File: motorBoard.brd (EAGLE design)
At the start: 160 x 100 mm, 58 parts

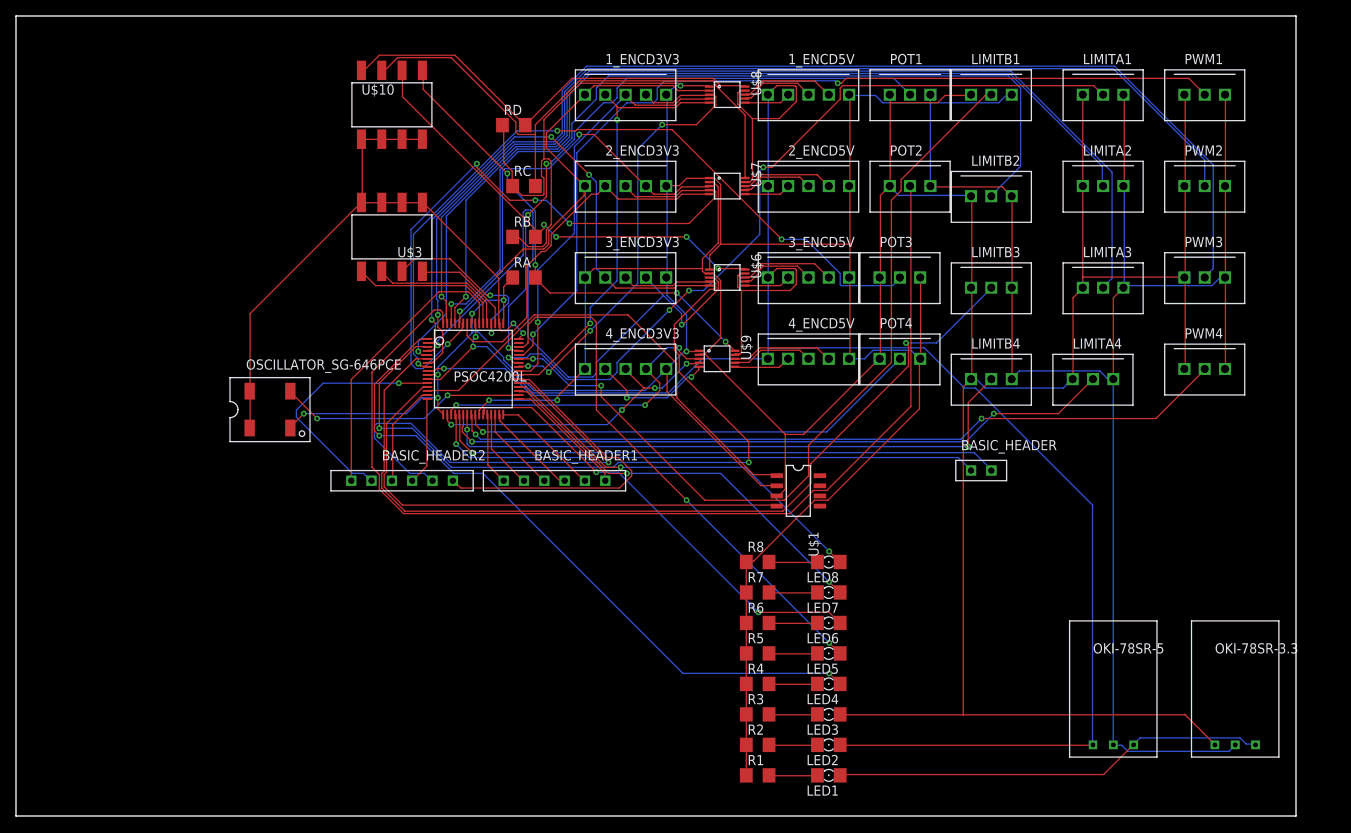
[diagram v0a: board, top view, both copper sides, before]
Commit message: Added decoupling caps, schematic tweaks, layout, mid routing
Running out of space around PSoC, so I need to rework my component layout.
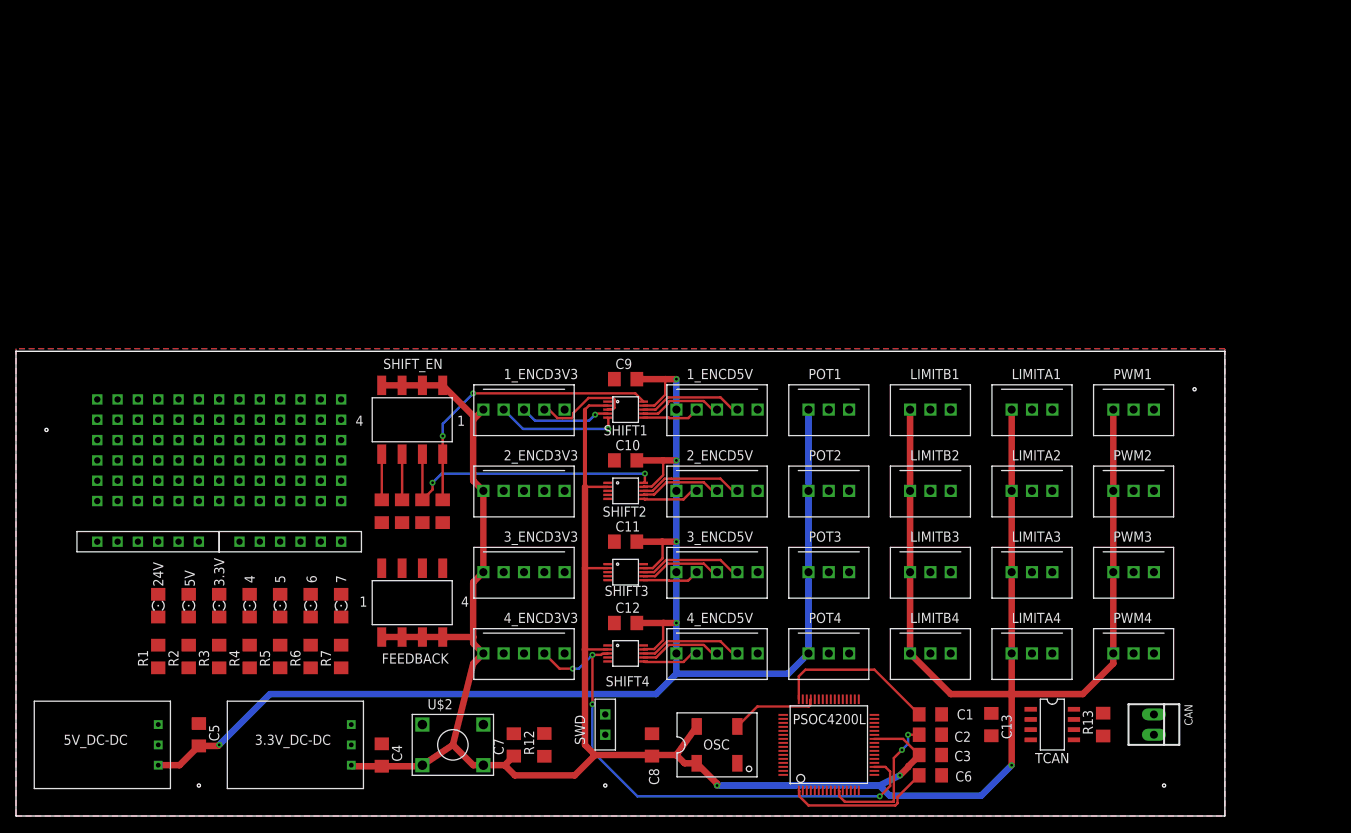
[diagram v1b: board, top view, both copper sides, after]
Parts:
- removed BASIC_HEADER: 2BASIC_HEADER, HuskyRobotics2017-18:2SIP_HEADER
- removed LED1, LED2, LED3, LED4, LED5, LED6, LED7, LED8: (no value), eagle-ltspice:LED_1206
- removed OKI-78SR-3.3: OKI-78SR-3.33SIP, HuskyRobotics2017-18:3SIP
- removed OKI-78SR-5: OKI-78SR-53SIP, HuskyRobotics2017-18:3SIP
- removed OSCILLATOR_SG-646PCE: ESPSON_SG-646PCE_CRYSTAL_OSCILLATOREPSON_SG-646PCE_32MHZ, HuskyRobotics2017-18:4SOJ-5.08MM
- removed RA, RB, RC, RD: 4.7k, eagle-ltspice:R1206
- removed U$10, U$3: SMD4SWSMD4SW, HuskyRobotics2017-18:GULL8
- removed U$6, U$7, U$8, U$9: LEVEL-SHIFTER_NVT2003DPNVT_2003DP_LEVEL_SHIFTER, HuskyRobotics2017-18:TSSOP10
- added 24V, 3.3V, 4, 5, 5V, 6, 7: (no value), eagle-ltspice:LED_1206
- added 3.3V_DC-DC: OKI-78SR-3.33SIP, HuskyRobotics2017-18:3SIP
- added 5V_DC-DC: OKI-78SR-53SIP, HuskyRobotics2017-18:3SIP
- added C1, C6: 1uF, eagle-ltspice:C1206
- added C10, C11, C12, C13, C2, C3, C7, C8, C9: 0.1uF, eagle-ltspice:C1206
- added C4, C5: 10uF, eagle-ltspice:C1206
- added CAN: 22-23-2021, con-molex:22-23-2021
- added FEEDBACK, SHIFT_EN: SMD4SWSMD4SW, HuskyRobotics2017-18:GULL8
- added OSC: ESPSON_SG-646PCE_CRYSTAL_OSCILLATOREPSON_SG-646PCE_32MHZ, HuskyRobotics2017-18:4SOJ-5.08MM
- added R10, R11, R12, R9: 4.7k, eagle-ltspice:R1206
- added R13: 120, eagle-ltspice:R1206
- added SHIFT1, SHIFT2, SHIFT3, SHIFT4: LEVEL-SHIFTER_NVT2003DPNVT_2003DP_LEVEL_SHIFTER, HuskyRobotics2017-18:TSSOP10
- added SWD: 2BASIC_HEADER, HuskyRobotics2017-18:2SIP_HEADER
- added TCAN: TCAN332TCAN332, HuskyRobotics2017-18:8SOIC3.9
- added U$2: PUSH_BUTTON, HuskyRobotics2017-18:PUSH_BUTTON
- R1: value (none) -> 1.2k
- R2: value (none) -> 150
- R3, R4, R5, R6, R7: value (none) -> 100
- R8: value (none) -> 4.7k
- U$1: value TCAN332TCAN332 -> OOPS_SPACE; device HuskyRobotics2017-18:8SOIC3.9 -> HuskyRobotics2017-18:OOPS_SPACE
- moved R1 76.4 mm to (17.8, 19.9), turned to 90 degrees
- moved U$1 72.6 mm to (25.4, 45.7), turned to 0 degrees
- moved R2 72.0 mm to (21.6, 19.9), turned to 90 degrees
- moved R3 67.7 mm to (25.4, 19.9), turned to 90 degrees
- moved PSOC4200L 64.7 mm to (101.6, 8.89), turned to 90 degrees
- moved R4 63.6 mm to (29.2, 19.9), turned to 90 degrees
- moved R5 59.7 mm to (33.0, 19.9), turned to 90 degrees
- moved R6 56.0 mm to (36.8, 19.9), turned to 90 degrees
- moved R7 52.7 mm to (40.6, 19.9), turned to 90 degrees
- moved BASIC_HEADER1 51.4 mm to (16.5, 34.3)
- moved R8 47.4 mm to (45.7, 38.1), turned to 90 degrees
- moved 1_ENCD3V3 41.4 mm to (63.5, 50.8)
- moved 1_ENCD5V 41.0 mm to (87.6, 50.8)
- moved POT1 40.7 mm to (101.6, 50.8)
- moved PWM1 40.4 mm to (139.7, 50.8)
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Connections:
- removed net LED8: LED8.A, PSOC4200L.36
- removed net N$23: LED8.C, R8.2
- new net VCCD: C1.1, PSOC4200L.48
- new net VREF: C6.2, PSOC4200L.1
- new net XRES: C7.2, PSOC4200L.47, R12.2, U$2.A1, U$2.A2
- net +24V: now also 24V.A, 3.3V_DC-DC.1, 5V_DC-DC.1; no longer LED1.A, OKI-78SR-3.3.1, OKI-78SR-5.1
- net +3V3: now also 3.3V.A, 3.3V_DC-DC.3, C13.2, C3.2, C4.2, C7.1, C8.2, FEEDBACK.1, FEEDBACK.2, FEEDBACK.3, FEEDBACK.4, OSC.1, OSC.4, SHIFT1.2, SHIFT2.2, SHIFT3.2, SHIFT4.2, SHIFT_EN.1, SHIFT_EN.2, SHIFT_EN.3, SHIFT_EN.4, TCAN.3, U$2.B1, U$2.B2; no longer LED3.A, OKI-78SR-3.3.3, OSCILLATOR_SG-646PCE.1, OSCILLATOR_SG-646PCE.4, POT1.1, POT2.1, POT3.1, POT4.1, PSOC4200L.48, PSOC4200L.50, U$1.3, U$10.1, U$10.2, U$10.3, U$10.4, U$3.1, U$3.2, U$3.3, U$3.4, U$6.2, U$7.2, U$8.2, U$9.2
- net +5V: now also 5V.A, 5V_DC-DC.3, C10.2, C11.2, C12.2, C2.2, C5.2, C9.2, POT1.1, POT2.1, POT3.1, POT4.1, PSOC4200L.50, SHIFT1.9, SHIFT2.9, SHIFT3.9, SHIFT4.9; no longer LED2.A, OKI-78SR-5.3, U$6.9, U$7.9, U$8.9, U$9.9
- net CANH: now also CAN.1, R13.2, TCAN.7; no longer U$1.7
- net CANL: now also CAN.2, R13.1, TCAN.6; no longer U$1.6
- net CANRX: now also TCAN.4; no longer U$1.4
- net CANTX: now also TCAN.1; no longer U$1.1
- net CLK_EXT: now also OSC.3; no longer OSCILLATOR_SG-646PCE.3
- net GNDA: now also 3.3V_DC-DC.2, 5V_DC-DC.2, C1.2, C10.1, C11.1, C12.1, C13.1, C2.1, C3.1, C4.1, C5.1, C6.1, C8.1, C9.1, OSC.2, R10.1, R11.1, R12.1, R9.1, SHIFT1.1, SHIFT2.1, SHIFT3.1, SHIFT4.1, TCAN.2; no longer OKI-78SR-3.3.2, OKI-78SR-5.2, OSCILLATOR_SG-646PCE.2, RA.1, RB.1, RC.1, RD.1, U$1.2, U$6.1, U$7.1, U$8.1, U$9.1
- net LED4: now also 4.A, PSOC4200L.36; no longer LED4.A, PSOC4200L.1
- net LED5: now also 5.A; no longer LED5.A
- net LED6: now also 6.A; no longer LED6.A
- net LED7: now also 7.A; no longer LED7.A
- net LEVEL_SHIFT_EN1: now also R11.2, SHIFT1.10, SHIFT_EN.8; no longer RD.2, U$10.8, U$8.10
- net LEVEL_SHIFT_EN2: now also R10.2, SHIFT2.10, SHIFT_EN.7; no longer RC.2, U$10.7, U$7.10
- net LEVEL_SHIFT_EN3: now also R9.2, SHIFT3.10, SHIFT_EN.6; no longer RB.2, U$10.6, U$6.10
- net LEVEL_SHIFT_EN4: now also R8.2, SHIFT4.10, SHIFT_EN.5; no longer RA.2, U$10.5, U$9.10
- net MOTOR1A1: now also SHIFT1.3; no longer U$8.3
- net MOTOR1A2: now also SHIFT1.4; no longer U$8.4
- net MOTOR1A3: now also SHIFT1.5; no longer U$8.5
- net MOTOR1B1: now also SHIFT1.8; no longer U$8.8
- net MOTOR1B2: now also SHIFT1.7; no longer U$8.7
- net MOTOR1B3: now also SHIFT1.6; no longer U$8.6
- net MOTOR2A1: now also SHIFT2.3; no longer U$7.3
- net MOTOR2A2: now also SHIFT2.4; no longer U$7.4
- net MOTOR2A3: now also SHIFT2.5; no longer U$7.5
- net MOTOR2B1: now also SHIFT2.8; no longer U$7.8
- net MOTOR2B2: now also SHIFT2.7; no longer U$7.7
- net MOTOR2B3: now also SHIFT2.6; no longer U$7.6
- net MOTOR3A1: now also SHIFT3.3; no longer U$6.3
- net MOTOR3A2: now also SHIFT3.4; no longer U$6.4
- net MOTOR3A3: now also SHIFT3.5; no longer U$6.5
- net MOTOR3B1: now also SHIFT3.8; no longer U$6.8
- net MOTOR3B2: now also SHIFT3.7; no longer U$6.7
- net MOTOR3B3: now also SHIFT3.6; no longer U$6.6
- net MOTOR4A1: now also SHIFT4.3; no longer U$9.3
- net MOTOR4A2: now also SHIFT4.4; no longer U$9.4
- net MOTOR4A3: now also SHIFT4.5; no longer U$9.5
- net MOTOR4B1: now also SHIFT4.8; no longer U$9.8
- net MOTOR4B2: now also SHIFT4.7; no longer U$9.7
- net MOTOR4B3: now also SHIFT4.6; no longer U$9.6
- net N$1: now also 24V.C; no longer LED1.C
- net N$10: now also 4.C; no longer LED4.C
- net N$13: now also 5.C; no longer LED5.C
- net N$17: now also 6.C; no longer LED6.C
- net N$20: now also 7.C; no longer LED7.C
- net N$4: now also 5V.C; no longer LED2.C
- net N$7: now also 3.3V.C; no longer LED3.C
- net SEL_SW1: now also FEEDBACK.8; no longer U$3.8
- net SEL_SW2: now also FEEDBACK.7; no longer U$3.7
- net SEL_SW3: now also FEEDBACK.6; no longer U$3.6
- net SEL_SW4: now also FEEDBACK.5; no longer U$3.5
- net SWD_CLK: now also SWD.2; no longer BASIC_HEADER.2
- net SWD_DATA: now also SWD.1; no longer BASIC_HEADER.1
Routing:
- net GNDA: track 576.6 -> 0.00 mm, vias 7 -> 0
- net MOTOR3PWM: track 147.2 -> 0.00 mm, vias 1 -> 0
- net +3V3: track 515.7 -> 370.0 mm, vias 4 -> 3
- net MOTOR3LIMA: track 133.7 -> 0.00 mm, vias 1 -> 0
- net MOTOR2POT: track 129.4 -> 0.00 mm
- net MOTOR2PWM: track 127.7 -> 0.00 mm, vias 1 -> 0
- net MOTOR1PWM: track 112.9 -> 0.00 mm, vias 2 -> 0
- net MOTOR2LIMA: track 112.5 -> 0.00 mm, vias 1 -> 0
- net MOTOR3LIMB: track 111.9 -> 0.00 mm, vias 1 -> 0
- net MOTOR2LIMB: track 110.3 -> 0.00 mm, vias 1 -> 0
- net MOTOR1LIMB: track 103.2 -> 0.00 mm, vias 2 -> 0
- net MOTOR3A2: track 102.8 -> 0.00 mm, vias 2 -> 0
- net MOTOR1LIMA: track 99.2 -> 0.00 mm, vias 4 -> 0
- net MOTOR4PWM: track 97.8 -> 0.00 mm, vias 2 -> 0
- net MOTOR3POT: track 93.3 -> 0.00 mm, vias 3 -> 0
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- added copper zone on layer 1, net GNDA
- added copper zone on layer 16, net GNDA
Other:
- board size 160 x 100 mm -> 151.1 x 58.1 mm
- board text added: "C"
- board text added: "D"
- board text added: "R8...11"

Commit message: 3x5in board, more room for better routing
Worked on routing
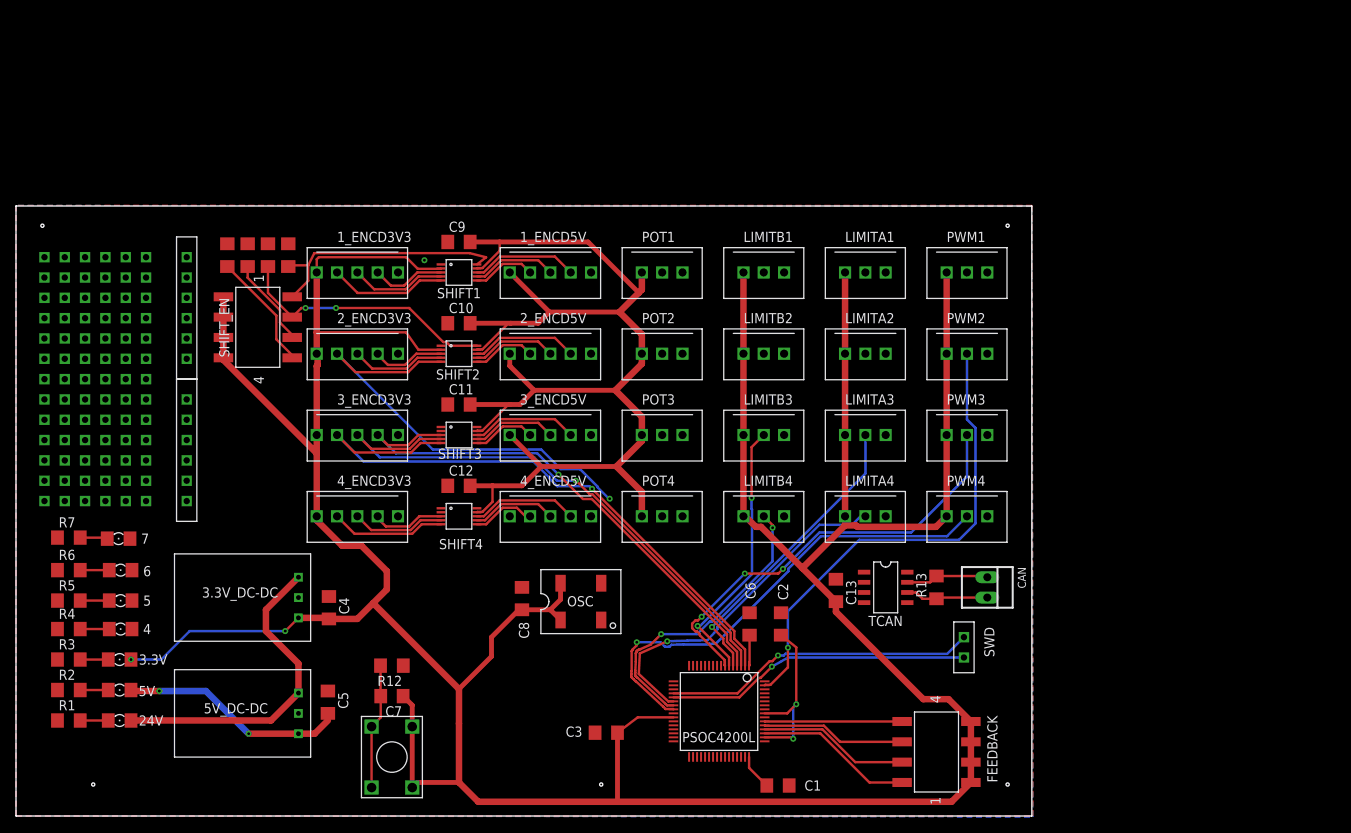
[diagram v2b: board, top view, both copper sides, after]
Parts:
- moved FEEDBACK 68.1 mm to (115.1, 8.00), turned to 90 degrees
- moved SWD 45.9 mm to (118.5, 21.1), turned to 270 degrees
- moved C3 40.6 mm to (73.8, 10.4), turned to 0 degrees
- moved R10 37.4 mm to (31.5, 70.1), turned to 270 degrees
- moved R11 37.4 mm to (34.0, 70.1), turned to 270 degrees
- moved R8 37.4 mm to (26.4, 70.1), turned to 270 degrees
- moved R9 37.4 mm to (29.0, 70.1), turned to 270 degrees
- moved R7 37.1 mm to (6.60, 34.8), turned to 0 degrees
- moved R6 32.1 mm to (6.60, 30.7), turned to 0 degrees
- moved BASIC_HEADER2 32.0 mm to (21.3, 63.5), turned to 90 degrees
- moved C6 29.5 mm to (91.7, 24.0), turned to 270 degrees
- moved 7 29.0 mm to (12.8, 34.7), turned to 180 degrees
- moved R5 27.3 mm to (6.60, 26.9), turned to 0 degrees
- moved 4_ENCD3V3 27.0 mm to (42.7, 37.5)
- moved C11 27.0 mm to (55.4, 51.4)
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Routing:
- net +3V3: track 370.0 -> 450.2 mm, vias 3 -> 2
- net MOTOR3A3: track 0.00 -> 79.1 mm, vias 0 -> 1
- net MOTOR3A2: track 0.00 -> 73.3 mm, vias 0 -> 1
- net MOTOR3A1: track 0.00 -> 67.4 mm, vias 0 -> 1
- net MOTOR2PWM: track 0.00 -> 60.5 mm, vias 0 -> 1
- net MOTOR4PWM: track 0.00 -> 59.9 mm, vias 0 -> 1
- net MOTOR4A1: track 65.6 -> 9.11 mm, vias 4 -> 0
- net MOTOR2A3: track 0.00 -> 56.1 mm, vias 0 -> 1
- net MOTOR3PWM: track 0.00 -> 54.3 mm, vias 0 -> 3
- net MOTOR4LIMA: track 0.00 -> 43.4 mm, vias 0 -> 1
- net +24V: track 0.00 -> 40.2 mm
- net SWD_DATA: track 0.00 -> 39.2 mm, vias 0 -> 1
- net SWD_CLK: track 0.00 -> 38.2 mm, vias 0 -> 1
- net MOTOR3LIMA: track 0.00 -> 37.9 mm, vias 0 -> 1
- net MOTOR4LIMB: track 0.00 -> 37.0 mm, vias 0 -> 2
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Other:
- board size 151.1 x 58.1 mm -> 127 x 76.3 mm
